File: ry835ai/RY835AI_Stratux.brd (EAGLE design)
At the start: 65 x 56 mm, 2 parts, among them X1 RASPI_BOARD_B+_HD

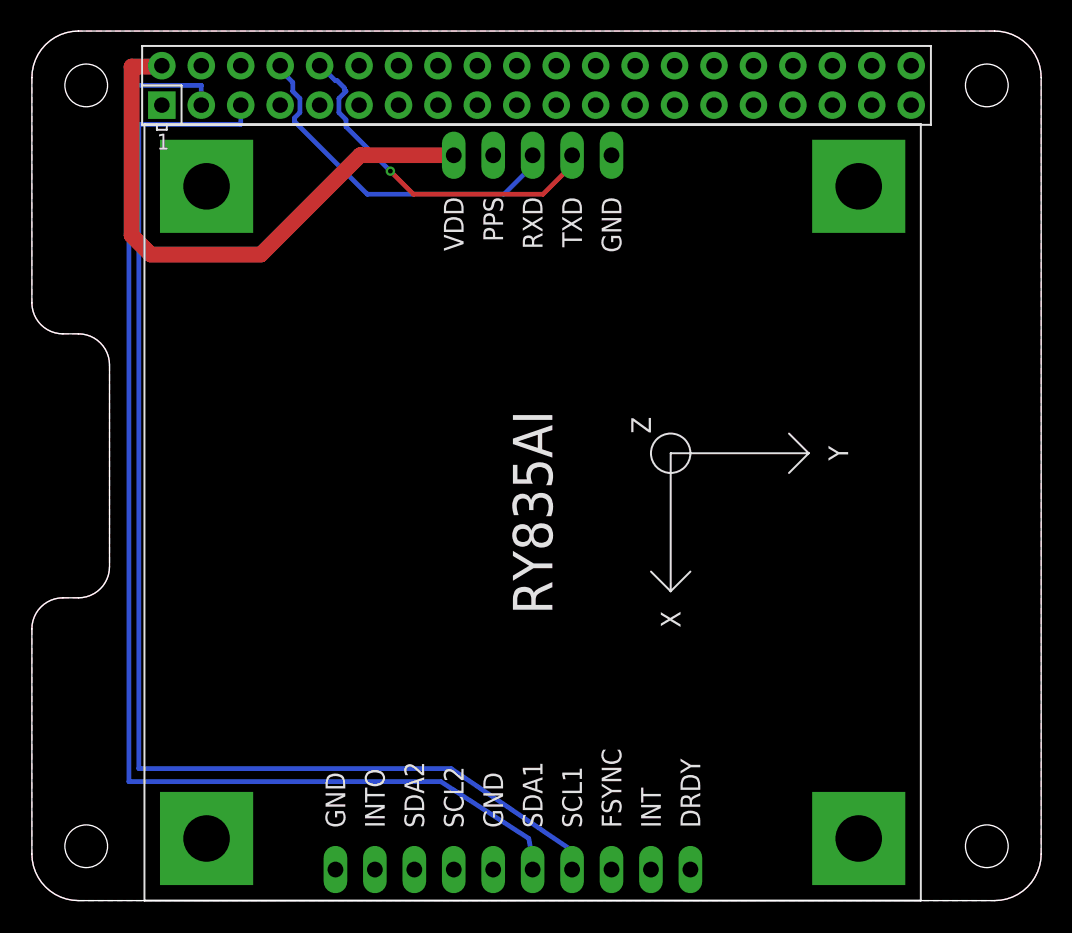
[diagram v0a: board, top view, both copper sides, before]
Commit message: Added bypass caps and cut-jumper for FSYNC signal. Added image to readme.md
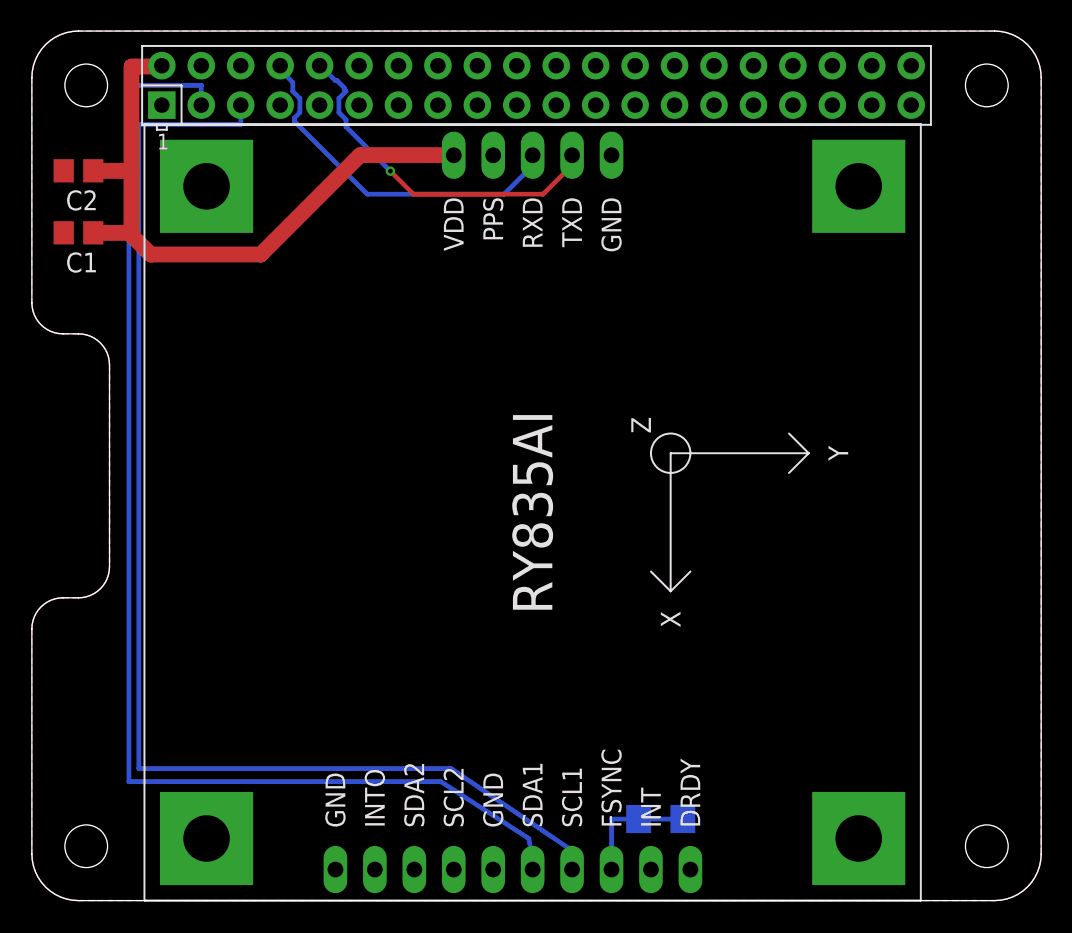
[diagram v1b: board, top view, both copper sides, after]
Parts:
- added C1: 10uF, rcl:C0805
- added C2: 0.1uF, rcl:C0805
- added FSYNC-GND: (no value), jblib:R1206-CUTJUMPER
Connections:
- new net N$3: FSYNC-GND.2, U$1.FSYNC
- net +5V: now also C1.1, C2.1
- net GND: now also C1.2, C2.2, FSYNC-GND.1; no longer U$1.FSYNC
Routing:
- net N$3: track 0.00 -> 5.00 mm
- net +5V: track 36.8 -> 41.7 mm
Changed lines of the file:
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@@
 <grid distance="1" unitdist="mm" unit="mm" style="lines" multiple="1" display="no" altdistance="0.25" altunitdist="mm" altunit="mm"/>
 <layers>
-<layer number="1" name="Top" color="4" fill="1" visible="yes" active="yes"/>
+<layer number="1" name="Top" color="4" fill="1" visible="no" active="yes"/>
 <layer number="16" name="Bottom" color="1" fill="1" visible="yes" active="yes"/>
 <layer number="17" name="Pads" color="2" fill="1" visible="yes" active="yes"/>
 <layer number="18" name="Vias" color="2" fill="1" visible="yes" active="yes"/>
-<layer number="19" name="Unrouted" color="6" fill="1" visible="yes" active="yes"/>
+<layer number="19" name="Unrouted" color="6" fill="1" visible="no" active="yes"/>
 <layer number="20" name="Dimension" color="15" fill="1" visible="yes" active="yes"/>
-<layer number="21" name="tPlace" color="7" fill="1" visible="yes" active="yes"/>
+<layer number="21" name="tPlace" color="7" fill="1" visible="no" active="yes"/>
 <layer number="22" name="bPlace" color="7" fill="1" visible="yes" active="yes"/>
-<layer number="23" name="tOrigins" color="15" fill="1" visible="yes" active="yes"/>
+<layer number="23" name="tOrigins" color="15" fill="1" visible="no" active="yes"/>
 <layer number="24" name="bOrigins" color="15" fill="1" visible="yes" active="yes"/>
 <layer number="25" name="tNames" color="7" fill="1" visible="no" active="yes"/>
-<layer number="26" name="bNames" color="7" fill="1" visible="no" active="yes"/>
+<layer number="26" name="bNames" color="7" fill="1" visible="yes" active="yes"/>
 <layer number="27" name="tValues" color="7" fill="1" visible="no" active="yes"/>
 <layer number="28" name="bValues" color="7" fill="1" visible="no" active="yes"/>
 <layer number="29" name="tStop" color="7" fill="3" visible="no" active="yes"/>
-<layer number="30" name="bStop" color="7" fill="6" visible="no" active="yes"/>
+<layer number="30" name="bStop" color="7" fill="6" visible="yes" active="yes"/>
 <layer number="31" name="tCream" color="7" fill="4" visible="no" active="yes"/>
 <layer number="32" name="bCream" color="7" fill="5" visible="no" active="yes"/>
@@
 <layer number="48" name="Document" color="7" fill="1" visible="no" active="yes"/>
 <layer number="49" name="Reference" color="7" fill="1" visible="no" active="yes"/>
-<layer number="51" name="tDocu" color="7" fill="1" visible="yes" active="yes"/>
-<layer number="52" name="bDocu" color="7" fill="1" visible="yes" active="yes"/>
+<layer number="50" name="dxf" color="7" fill="1" visible="no" active="yes"/>
+<layer number="51" name="tDocu" color="7" fill="1" visible="no" active="yes"/>
+<layer number="52" name="bDocu" color="7" fill="1" visible="no" active="yes"/>
+<layer number="53" name="tGND_GNDA" color="7" fill="9" visible="no" active="no"/>
+<layer number="54" name="bGND_GNDA" color="1" fill="9" visible="no" active="no"/>
+<layer number="56" name="wert" color="7" fill="1" visible="no" active="no"/>
 <layer number="90" name="Modules" color="5" fill="1" visible="no" active="no"/>
 <layer number="91" name="Nets" color="2" fill="1" visible="no" active="no"/>
@@
 <layer number="97" name="Info" color="7" fill="1" visible="no" active="no"/>
 <layer number="98" name="Guide" color="6" fill="1" visible="no" active="no"/>
+<layer number="100" name="Muster" color="7" fill="1" visible="no" active="no"/>
+<layer number="101" name="Patch_Top" color="12" fill="4" visible="no" active="yes"/>
+<layer number="102" name="Vscore" color="7" fill="1" visible="no" active="yes"/>
+<layer number="103" name="tMap" color="7" fill="1" visible="no" active="yes"/>
+<layer number="104" name="Name" color="16" fill="1" visible="no" active="yes"/>
+<layer number="105" name="tPlate" color="7" fill="1" visible="no" active="yes"/>
+<layer number="106" name="bPlate" color="7" fill="1" visible="no" active="yes"/>
+<layer number="107" name="Crop" color="7" fill="1" visible="no" active="yes"/>
+<layer number="116" name="Patch_BOT" color="9" fill="4" visible="no" active="yes"/>
+<layer number="121" name="_tsilk" color="7" fill="1" visible="no" active="yes"/>
+<layer number="122" name="_bsilk" color="7" fill="1" visible="no" active="yes"/>
+<layer number="125" name="_tNames" color="7" fill="1" visible="no" active="yes"/>
+<layer number="144" name="Drill_legend" color="7" fill="1" visible="no" active="yes"/>
+<layer number="151" name="HeatSink" color="7" fill="1" visible="no" active="yes"/>
+<layer number="200" name="200bmp" color="1" fill="10" visible="no" active="yes"/>
+<layer number="201" name="201bmp" color="2" fill="10" visible="no" active="yes"/>
+<layer number="202" name="202bmp" color="3" fill="10" visible="no" active="yes"/>
+<layer number="203" name="203bmp" color="4" fill="10" visible="no" active="yes"/>
+<layer number="204" name="204bmp" color="5" fill="10" visible="no" active="yes"/>
+<layer number="205" name="205bmp" color="6" fill="10" visible="no" active="yes"/>
+<layer number="206" name="206bmp" color="7" fill="10" visible="no" active="yes"/>
+<layer number="207" name="207bmp" color="8" fill="10" visible="no" active="yes"/>
+<layer number="208" name="208bmp" color="9" fill="10" visible="no" active="yes"/>
+<layer number="209" name="209bmp" color="7" fill="1" visible="no" active="yes"/>
+<layer number="210" name="210bmp" color="7" fill="1" visible="no" active="yes"/>
+<layer number="211" name="211bmp" color="7" fill="1" visible="no" active="yes"/>
+<layer number="212" name="212bmp" color="7" fill="1" visible="no" active="yes"/>
+<layer number="213" name="213bmp" color="7" fill="1" visible="no" active="yes"/>
+<layer number="214" name="214bmp" color="7" fill="1" visible="no" active="yes"/>
+<layer number="215" name="215bmp" color="7" fill="1" visible="no" active="yes"/>
+<layer number="216" name="216bmp" color="7" fill="1" visible="no" active="yes"/>
+<layer number="217" name="217bmp" color="18" fill="1" visible="no" active="no"/>
+<layer number="218" name="218bmp" color="19" fill="1" visible="no" active="no"/>
+<layer number="219" name="219bmp" color="20" fill="1" visible="no" active="no"/>
+<layer number="220" name="220bmp" color="21" fill="1" visible="no" active="no"/>
+<layer number="221" name="221bmp" color="22" fill="1" visible="no" active="no"/>
+<layer number="222" name="222bmp" color="23" fill="1" visible="no" active="no"/>
+<layer number="223" name="223bmp" color="24" fill="1" visible="no" active="no"/>
+<layer number="224" name="224bmp" color="25" fill="1" visible="no" active="no"/>
+<layer number="250" name="Descript" color="7" fill="1" visible="no" active="yes"/>
+<layer number="251" name="SMDround" color="7" fill="1" visible="no" active="yes"/>
+<layer number="254" name="cooling" color="7" fill="1" visible="no" active="yes"/>
 </layers>
 <board>
@@
 <description language="de">&lt;b&gt;EAGLE Design Rules&lt;/b&gt;
 &lt;p&gt;
-Die Standard-Design-Rules sind so gewÃ¤hlt, dass sie fÃ¼r
+Die Standard-Design-Rules sind so gewÃÂ¤hlt, dass sie fÃÂ¼r
 die meisten Anwendungen passen. Sollte ihre Platine
 besondere Anforderungen haben, treffen Sie die erforderlichen
@@
 <autorouter>
 <pass name="Default">
-<param name="RoutingGrid" value="6.25mil"/>
+<param name="RoutingGrid" value="0.125mm"/>
 <param name="AutoGrid" value="1"/>
 <param name="Efforts" value="1"/>
@@
 <element name="X1" library="raspberrypi_bastelstube_v13" package="RASPI_BOARD_B+HAT_DF" value="RASPI_BOARD_B+_HD" x="0" y="0"/>
 <element name="U$1" library="RY835AI" package="RY835AI" value="RY835AI" x="32.25" y="25" rot="SR270"/>
+<element name="C1" library="rcl" package="C0805" value="10uF" x="3" y="43" rot="R180"/>
+<element name="C2" library="rcl" package="C0805" value="0.1uF" x="3" y="47" rot="R180"/>
+<element name="FSYNC-GND" library="jblib" package="R1206-CUTJUMPER" value="" x="40.5" y="5.25" rot="MR0"/>
 </elements>
 <signals>
@@
 <contactref element="U$1" pad="GND@6"/>
 <contactref element="U$1" pad="GND@7"/>
-<contactref element="U$1" pad="FSYNC"/>
 <contactref element="X1" pad="9"/>
 <contactref element="X1" pad="25"/>
@@
 <contactref element="X1" pad="20"/>
 <contactref element="X1" pad="39"/>
+<contactref element="C2" pad="2"/>
+<contactref element="C1" pad="2"/>
+<contactref element="FSYNC-GND" pad="1"/>
 </signal>
 <signal name="+5V" class="1">
@@
 <wire x1="7.6581" y1="41.6052" x2="14.7447" y2="41.6052" width="1.016" layer="1"/>
 <wire x1="6.4222" y1="42.8411" x2="7.6581" y2="41.6052" width="1.016" layer="1"/>
-<wire x1="6.4222" y1="53.7137" x2="6.4222" y2="42.8411" width="1.016" layer="1"/>
+<wire x1="6.4222" y1="53.7137" x2="6.4222" y2="47" width="1.016" layer="1"/>
+<wire x1="6.4222" y1="47" x2="6.4222" y2="43" width="1.016" layer="1"/>
+<wire x1="6.4222" y1="43" x2="6.4222" y2="42.8411" width="1.016" layer="1"/>
 <wire x1="27.0891" y1="48.006" x2="27.17" y2="48" width="1.016" layer="1"/>
 <wire x1="6.4222" y1="53.7137" x2="8.37" y2="53.7137" width="1.016" layer="1"/>
 <wire x1="8.37" y1="53.7137" x2="8.37" y2="53.77" width="1.016" layer="1"/>
+<contactref element="C2" pad="1"/>
+<contactref element="C1" pad="1"/>
+<wire x1="6.4222" y1="43" x2="3.95" y2="43" width="1.016" layer="1"/>
+<wire x1="6.4222" y1="47" x2="3.95" y2="47" width="1.016" layer="1"/>
 </signal>
 <signal name="N$1">
@@
 <via x="23.0886" y="46.9773" extent="1-16" drill="0.3048"/>
 </signal>
+<signal name="N$3">
+<contactref element="U$1" pad="FSYNC"/>
+<contactref element="FSYNC-GND" pad="2"/>
+<wire x1="39.078" y1="5.25" x2="37.33" y2="5.25" width="0.3048" layer="16"/>
+<wire x1="37.33" y1="5.25" x2="37.33" y2="2" width="0.3048" layer="16"/>
+</signal>
 </signals>

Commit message: Keepout area added underneith GPS antenna area. Pads around mount points redeuced and made round to make room for signal traces.
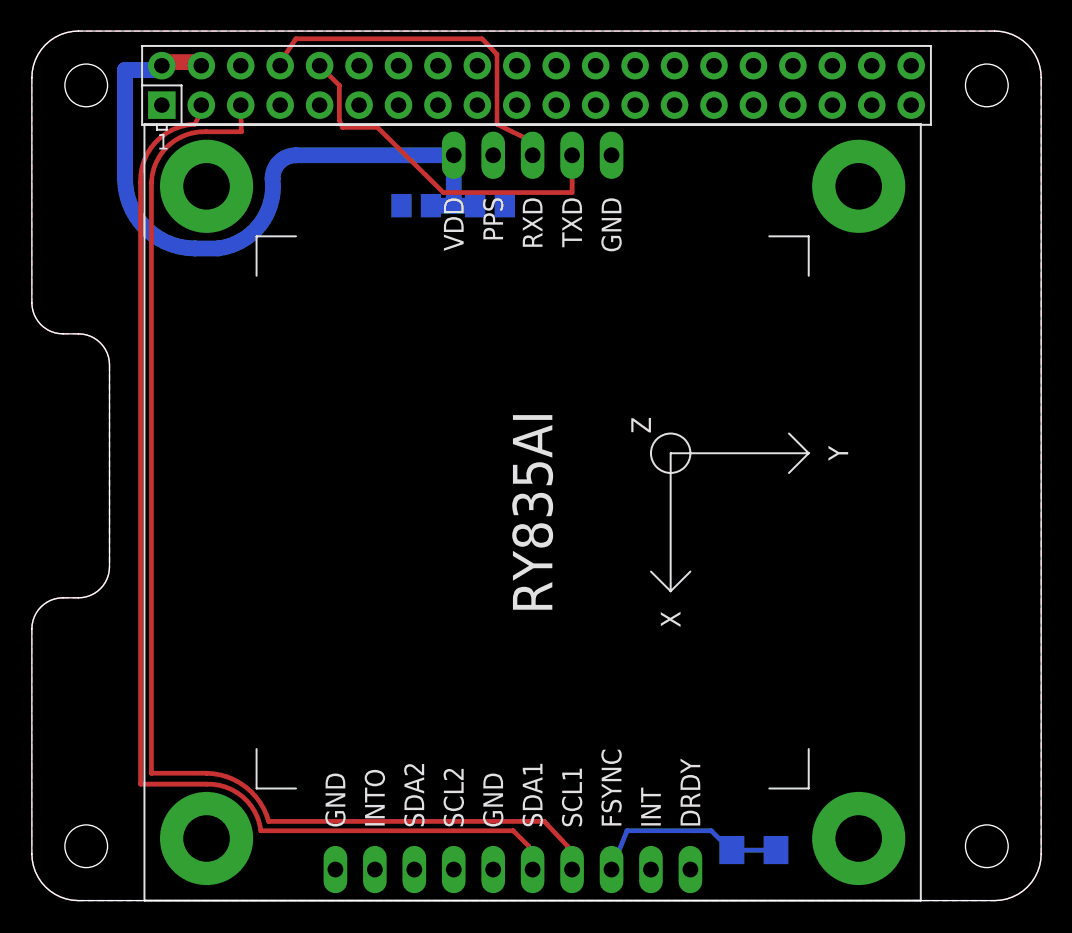
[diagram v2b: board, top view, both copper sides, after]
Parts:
- X2: value RASPI_BOARD_B+_HD -> RASPI_BOARD_B+#_HD
- moved C1 26.6 mm to (29.5, 44.8), flipped to the bottom
- moved C2 21.9 mm to (24.8, 44.8), flipped to the bottom, turned to 0 degrees
- moved FSYNC-GND 6.32 mm to (46.5, 3.25)
- renumbered X1 to X2
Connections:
- net +3V3 renamed 3V3A
- new net 3V3B: X2.17
- net +5V: now also X2.4
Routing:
- net N$1: track 79.6 -> 73.5 mm
- net N$3: track 5.00 -> 10.1 mm
- net N$2: track 80.1 -> 77.2 mm
- net +5V: track 41.7 -> 44.1 mm
- net RXTX_BUS1: track 22.9 -> 23.5 mm, vias 1 -> 0

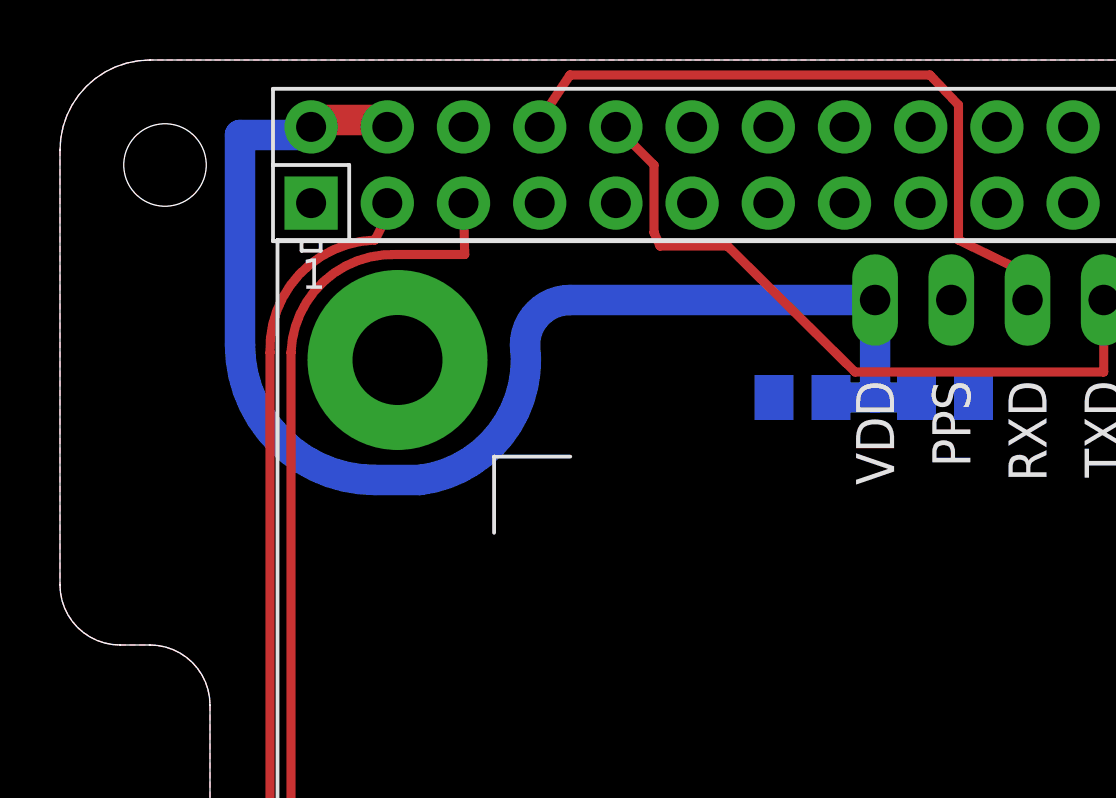
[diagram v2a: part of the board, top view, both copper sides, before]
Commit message: added fan control
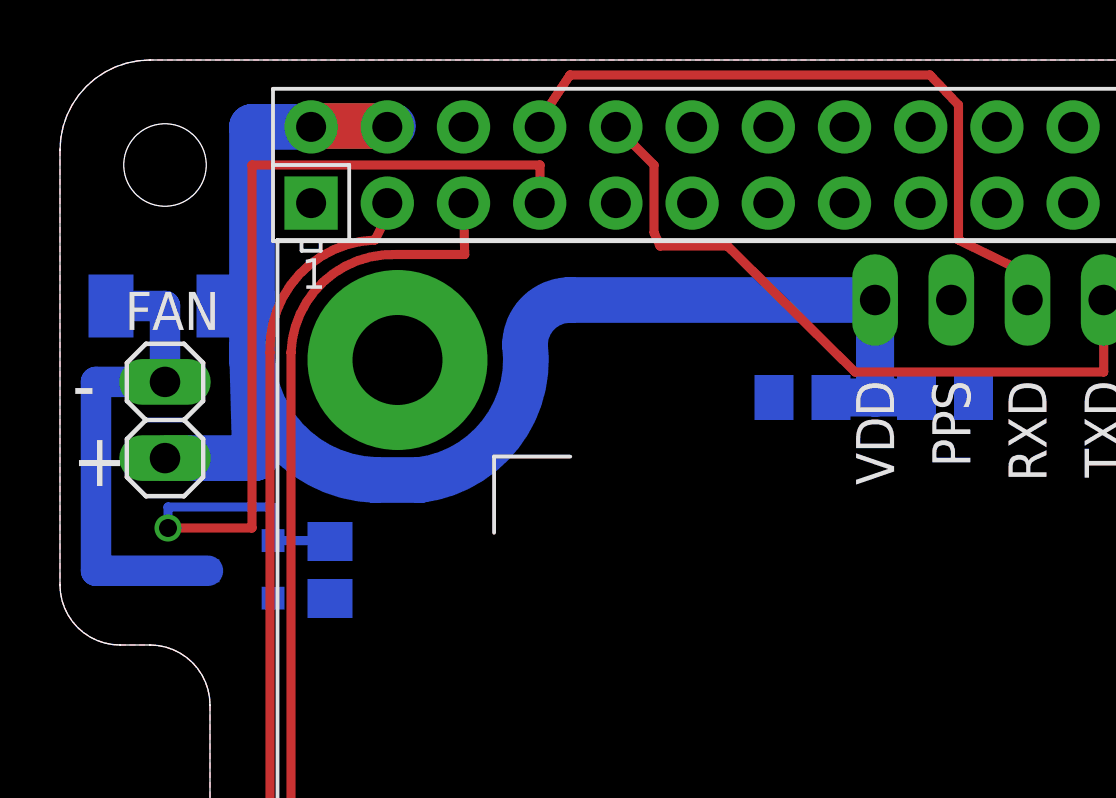
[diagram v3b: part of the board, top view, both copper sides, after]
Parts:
- added D1: CGRM4001-G, diode:SOD-123_MINI-SMA
- added FAN: (no value), pinhead:1X02
- added Q1: (no value), transistors:SOT-23
- added R1: (no value), resistor:R0805
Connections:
- new net FAN_GPIO: Q1.1, R1.2, X2.7
- new net N$4: D1.A, FAN.2, Q1.3
- net +5V: now also D1.C, FAN.1
- net GND: now also Q1.2, R1.1
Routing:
- net FAN_GPIO: track 0.00 -> 33.0 mm, vias 0 -> 1
- net N$4: track 0.00 -> 16.7 mm
- net +5V: track 44.1 -> 54.3 mm
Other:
- board text added: "+"
- board text added: "-"
- board text added: "USE AT YOUR OWN RISK! THIS BOARD IS PROVIDED "AS IS", WITHOUT WARRANTY OF ANY KIND, EXPRESS OR IMPLIED. The copyright holder disclaims all liability for damages resulting from use of this board to the fullest extent possible."
